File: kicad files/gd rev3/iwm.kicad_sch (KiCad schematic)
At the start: 24 parts, among them J2 DB19_4, J3 DB19_16, J4 EN, J5 DSUB19, J6 FDC Hdr, J7 EN, J8 EN, J9 Game Port, U11 IWM

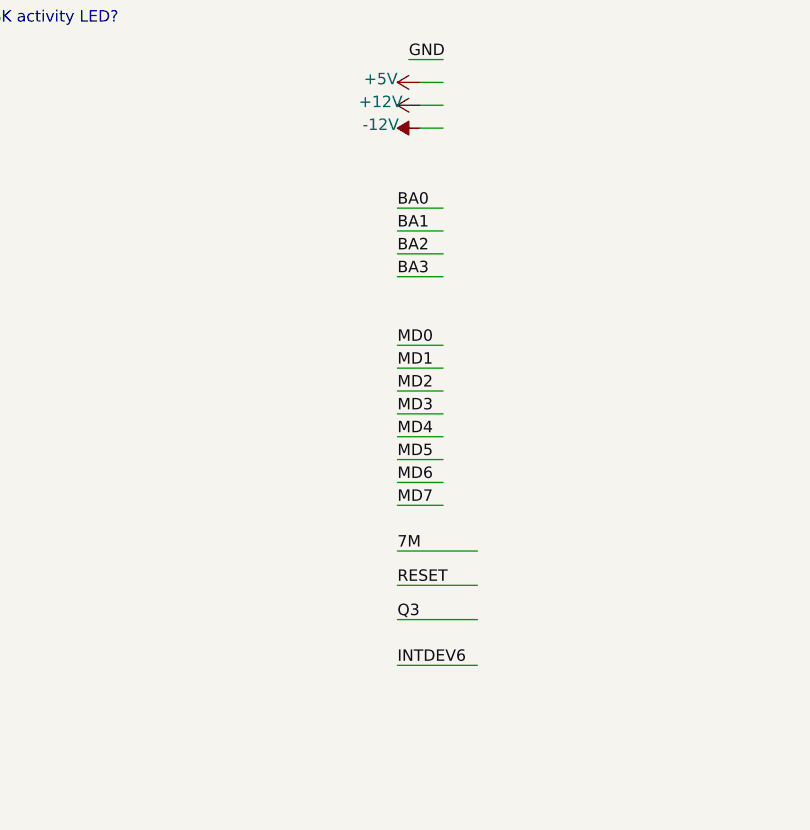
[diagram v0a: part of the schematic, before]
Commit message: ibom for audio and adding some hierarchical labels (wrong branch)
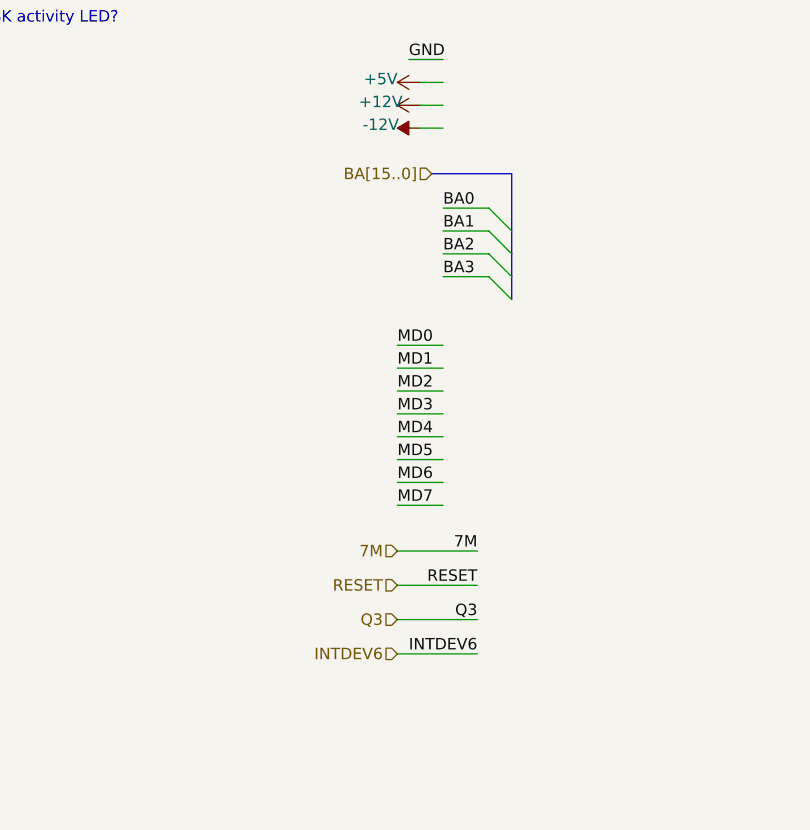
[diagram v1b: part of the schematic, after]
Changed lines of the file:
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@@
   )
   (no_connect (at 339.09 106.68))
+  (bus_entry (at 33.02 78.74) (size 2.54 2.54)
+    (stroke (width 0) (type default) (color 0 0 0 0))
+  )
+  (bus_entry (at 33.02 76.2) (size 2.54 2.54)
+    (stroke (width 0) (type default) (color 0 0 0 0))
+  )
+  (bus_entry (at 33.02 81.28) (size 2.54 2.54)
+    (stroke (width 0) (type default) (color 0 0 0 0))
+  )
+  (bus_entry (at 33.02 73.66) (size 2.54 2.54)
+    (stroke (width 0) (type default) (color 0 0 0 0))
+  )
   (wire (pts (xy 229.87 68.58) (xy 229.87 74.93))
     (stroke (width 0) (type default) (color 0 0 0 0))
@@
     (stroke (width 0) (type default) (color 0 0 0 0))
   )
-  (wire (pts (xy 22.86 76.2) (xy 27.94 76.2))
+  (wire (pts (xy 27.94 76.2) (xy 33.02 76.2))
     (stroke (width 0) (type default) (color 0 0 0 0))
   )
@@
     (stroke (width 0) (type default) (color 0 0 0 0))
   )
+  (bus (pts (xy 35.56 83.82) (xy 35.56 81.28))
+    (stroke (width 0) (type default) (color 0 0 0 0))
+  )
   (wire (pts (xy 201.93 110.49) (xy 212.09 110.49))
     (stroke (width 0) (type default) (color 0 0 0 0))
@@
     (stroke (width 0) (type default) (color 0 0 0 0))
   )
+  (bus (pts (xy 35.56 81.28) (xy 35.56 78.74))
+    (stroke (width 0) (type default) (color 0 0 0 0))
+  )
   (wire (pts (xy 209.55 102.87) (xy 209.55 105.41))
     (stroke (width 0) (type default) (color 0 0 0 0))
@@
     (stroke (width 0) (type default) (color 0 0 0 0))
   )
+  (bus (pts (xy 26.67 69.85) (xy 35.56 69.85))
+    (stroke (width 0) (type default) (color 0 0 0 0))
+  )
   (wire (pts (xy 227.33 53.34) (xy 227.33 60.96))
     (stroke (width 0) (type default) (color 0 0 0 0))
@@
     (stroke (width 0) (type default) (color 0 0 0 0))
   )
-  (wire (pts (xy 22.86 78.74) (xy 27.94 78.74))
+  (wire (pts (xy 27.94 78.74) (xy 33.02 78.74))
     (stroke (width 0) (type default) (color 0 0 0 0))
   )
@@
     (stroke (width 0) (type default) (color 0 0 0 0))
   )
+  (bus (pts (xy 35.56 76.2) (xy 35.56 69.85))
+    (stroke (width 0) (type default) (color 0 0 0 0))
+  )
   (wire (pts (xy 339.09 121.92) (xy 344.17 121.92))
     (stroke (width 0) (type default) (color 0 0 0 0))
@@
     (stroke (width 0) (type default) (color 0 0 0 0))
   )
-  (wire (pts (xy 22.86 81.28) (xy 27.94 81.28))
+  (wire (pts (xy 27.94 81.28) (xy 33.02 81.28))
     (stroke (width 0) (type default) (color 0 0 0 0))
   )
@@
     (stroke (width 0) (type default) (color 0 0 0 0))
   )
-  (wire (pts (xy 31.75 124.46) (xy 22.86 124.46))
+  (wire (pts (xy 31.75 123.19) (xy 22.86 123.19))
     (stroke (width 0) (type default) (color 0 0 0 0))
   )
@@
     (stroke (width 0) (type default) (color 0 0 0 0))
   )
+  (bus (pts (xy 35.56 78.74) (xy 35.56 76.2))
+    (stroke (width 0) (type default) (color 0 0 0 0))
+  )
   (wire (pts (xy 224.79 90.17) (xy 232.41 90.17))
     (stroke (width 0) (type default) (color 0 0 0 0))
@@
     (stroke (width 0) (type default) (color 0 0 0 0))
   )
-  (wire (pts (xy 22.86 73.66) (xy 27.94 73.66))
+  (wire (pts (xy 27.94 73.66) (xy 33.02 73.66))
     (stroke (width 0) (type default) (color 0 0 0 0))
   )
@@
     (effects (font (size 1.27 1.27)) (justify right bottom))
   )
-  (label "RESET" (at 22.86 115.57 0)
-    (effects (font (size 1.27 1.27)) (justify left bottom))
+  (label "RESET" (at 31.75 115.57 180)
+    (effects (font (size 1.27 1.27)) (justify right bottom))
   )
   (label "bWREQ" (at 229.87 60.96 90)
@@
     (effects (font (size 1.27 1.27)) (justify left bottom))
   )
-  (label "7M" (at 22.86 111.76 0)
-    (effects (font (size 1.27 1.27)) (justify left bottom))
+  (label "7M" (at 31.75 111.76 180)
+    (effects (font (size 1.27 1.27)) (justify right bottom))
   )
   (label "GND" (at 205.74 87.63 0)
@@
     (effects (font (size 1.27 1.27)) (justify right bottom))
   )
-  (label "BA1" (at 22.86 76.2 0)
+  (label "BA1" (at 27.94 76.2 0)
     (effects (font (size 1.27 1.27)) (justify left bottom))
   )
@@
     (effects (font (size 1.27 1.27)) (justify left bottom))
   )
-  (label "BA3" (at 22.86 81.28 0)
+  (label "BA3" (at 27.94 81.28 0)
     (effects (font (size 1.27 1.27)) (justify left bottom))
   )
@@
     (effects (font (size 1.27 1.27)) (justify right bottom))
   )
-  (label "BA0" (at 22.86 73.66 0)
+  (label "BA0" (at 27.94 73.66 0)
     (effects (font (size 1.27 1.27)) (justify left bottom))
   )
@@
     (effects (font (size 1.27 1.27)) (justify right bottom))
   )
-  (label "INTDEV6" (at 22.86 124.46 0)
-    (effects (font (size 1.27 1.27)) (justify left bottom))
+  (label "INTDEV6" (at 31.75 123.19 180)
+    (effects (font (size 1.27 1.27)) (justify right bottom))
   )
   (label "seek1" (at 143.51 101.6 180)
@@
     (effects (font (size 1.27 1.27)) (justify right bottom))
   )
-  (label "BA2" (at 22.86 78.74 0)
+  (label "BA2" (at 27.94 78.74 0)
     (effects (font (size 1.27 1.27)) (justify left bottom))
   )
@@
     (effects (font (size 1.27 1.27)) (justify right bottom))
   )
-  (label "Q3" (at 22.86 119.38 0)
-    (effects (font (size 1.27 1.27)) (justify left bottom))
+  (label "Q3" (at 31.75 119.38 180)
+    (effects (font (size 1.27 1.27)) (justify right bottom))
   )
   (label "PDL1" (at 344.17 121.92 180)
@@
     (effects (font (size 1.27 1.27)) (justify left bottom))
   )
+  (hierarchical_label "INTDEV6" (shape input) (at 22.86 123.19 180)
+    (effects (font (size 1.27 1.27)) (justify right))
+  )
+  (hierarchical_label "RESET" (shape input) (at 22.86 115.57 180)
+    (effects (font (size 1.27 1.27)) (justify right))
+  )
+  (hierarchical_label "Q3" (shape input) (at 22.86 119.38 180)
+    (effects (font (size 1.27 1.27)) (justify right))
+  )
+  (hierarchical_label "7M" (shape input) (at 22.86 111.76 180)
+    (effects (font (size 1.27 1.27)) (justify right))
+  )
+  (hierarchical_label "BA[15..0]" (shape input) (at 26.67 69.85 180)
+    (effects (font (size 1.27 1.27)) (justify right))
+  )
   (symbol (lib_id "power:+5V") (at 321.31 106.68 0) (unit 1)

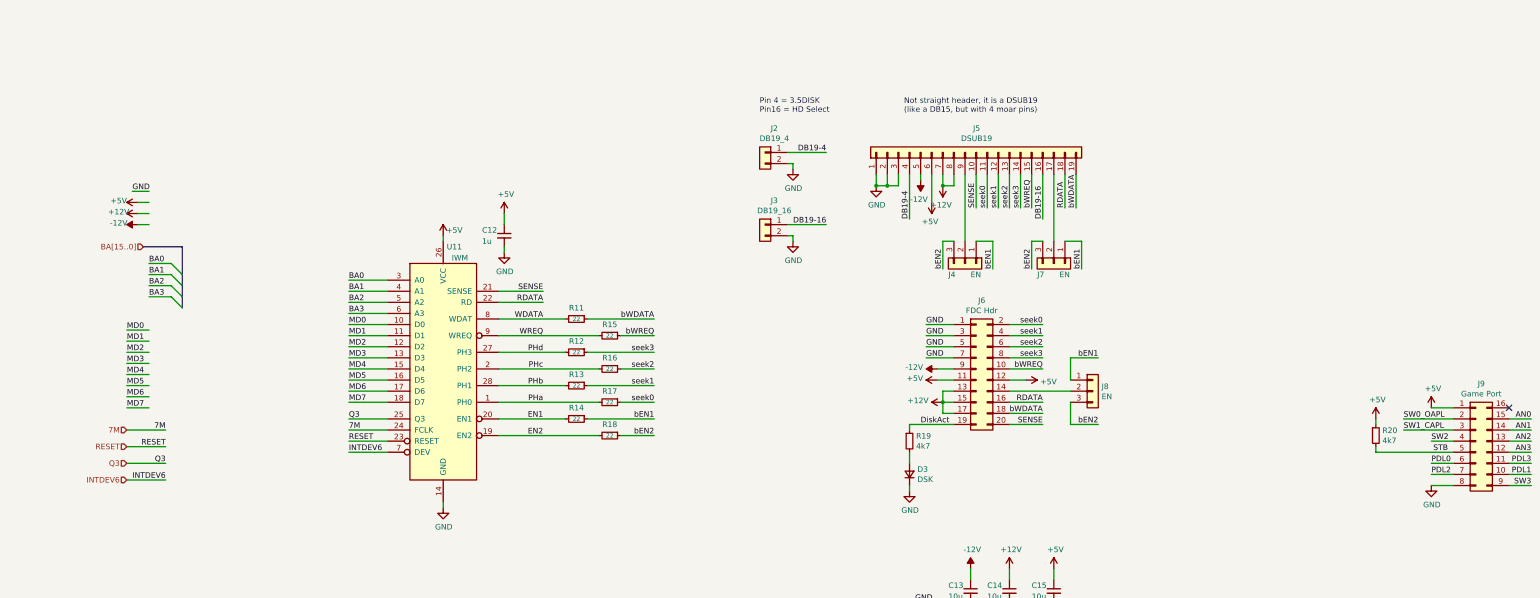
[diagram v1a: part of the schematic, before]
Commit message: initial slot/io breakout sheet labels
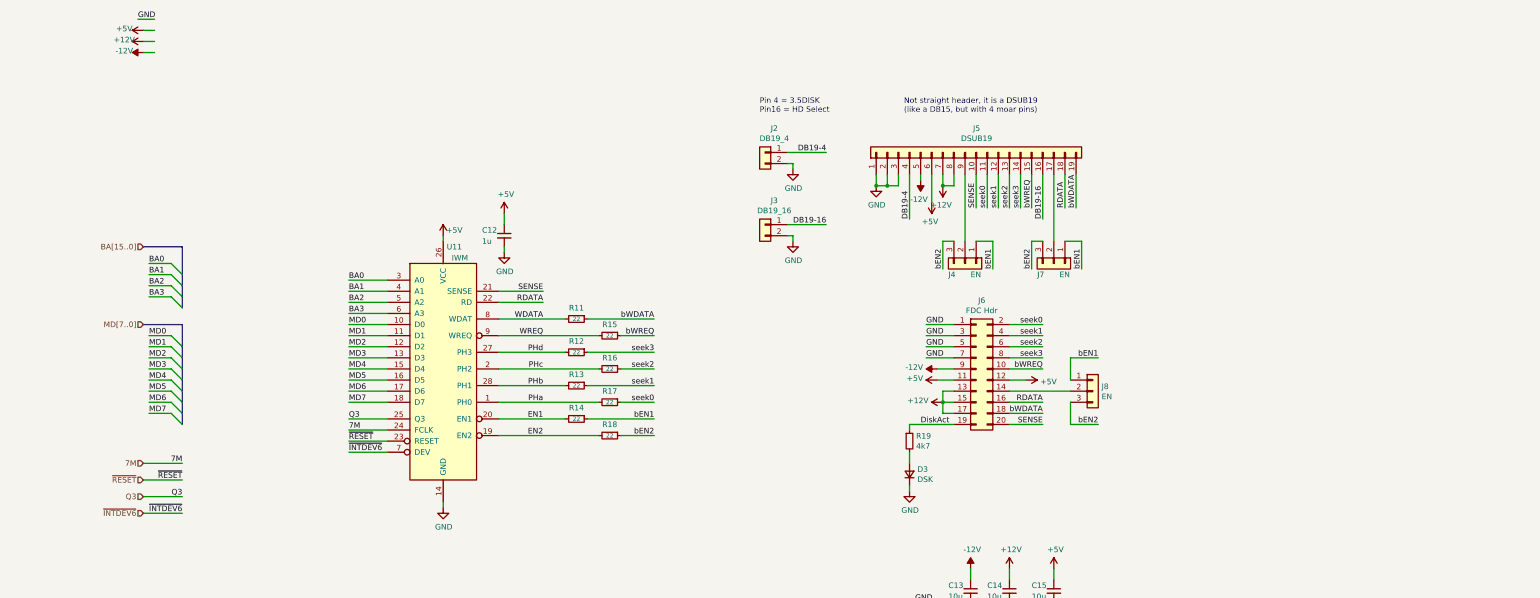
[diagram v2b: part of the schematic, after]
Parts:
- removed J9: Game Port, Package_DIP:DIP-16_W7.62mm_Socket, symbol Connector_Generic:Conn_02x08_Counter_Clockwise
- removed R20: 4k7, Resistor_SMD:R_0805_2012Metric, symbol My_Library:R_0805
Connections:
- net INTDEV6 renamed ~{INTDEV6}
- net RESET renamed ~{RESET}
- no-connect marks 1 -> 0

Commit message: after crash commit. arranging high-level sheet signals (and added audio circuit)
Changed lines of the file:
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@@
-    (stroke (width 0) (type default) (color 0 0 0 0))
-  )
-  (wire (pts (xy 25.4 17.78) (xy 29.21 17.78))
     (stroke (width 0) (type default) (color 0 0 0 0))
   )
@@
     (stroke (width 0) (type default) (color 0 0 0 0))
   )
-  (wire (pts (xy 29.21 25.4) (xy 26.67 25.4))
-    (stroke (width 0) (type default) (color 0 0 0 0))
-  )
   (wire (pts (xy 201.93 110.49) (xy 201.93 111.76))
     (stroke (width 0) (type default) (color 0 0 0 0))
@@
     (stroke (width 0) (type default) (color 0 0 0 0))
   )
-  (wire (pts (xy 26.67 22.86) (xy 29.21 22.86))
-    (stroke (width 0) (type default) (color 0 0 0 0))
-  )
   (wire (pts (xy 209.55 68.58) (xy 209.55 74.93))
     (stroke (width 0) (type default) (color 0 0 0 0))
@@
   )
   (wire (pts (xy 229.87 53.34) (xy 229.87 60.96))
-    (stroke (width 0) (type default) (color 0 0 0 0))
-  )
-  (wire (pts (xy 29.21 20.32) (xy 26.67 20.32))
     (stroke (width 0) (type default) (color 0 0 0 0))
   )
@@
   )
   (label "~{RESET}" (at 73.66 114.3 0)
-    (effects (font (size 1.27 1.27)) (justify left bottom))
-  )
-  (label "GND" (at 25.4 17.78 0)
     (effects (font (size 1.27 1.27)) (justify left bottom))
   )
@@
     )
     (property "Datasheet" "" (id 3) (at 109.22 62.23 0)
-      (effects (font (size 1.27 1.27)) hide)
-    )
-    (pin "1")
-  )
-  (symbol (lib_id "power:-12V") (at 26.67 25.4 90) (unit 1)
-    (in_bom yes) (on_board yes)
-    (property "Reference" "#PWR0181" (id 0) (at 24.13 25.4 0)
-      (effects (font (size 1.27 1.27)) hide)
-    )
-    (property "Value" "-12V" (id 1) (at 22.2758 25.019 90))
-    (property "Footprint" "" (id 2) (at 26.67 25.4 0)
-      (effects (font (size 1.27 1.27)) hide)
-    )
-    (property "Datasheet" "" (id 3) (at 26.67 25.4 0)
-      (effects (font (size 1.27 1.27)) hide)
-    )
-    (pin "1")
-  )
-  (symbol (lib_id "power:+12V") (at 26.67 22.86 90) (unit 1)
-    (in_bom yes) (on_board yes)
-    (property "Reference" "#PWR0180" (id 0) (at 30.48 22.86 0)
-      (effects (font (size 1.27 1.27)) hide)
-    )
-    (property "Value" "+12V" (id 1) (at 22.2758 22.479 90))
-    (property "Footprint" "" (id 2) (at 26.67 22.86 0)
-      (effects (font (size 1.27 1.27)) hide)
-    )
-    (property "Datasheet" "" (id 3) (at 26.67 22.86 0)
       (effects (font (size 1.27 1.27)) hide)
     )
@@
     (pin "9")
   )
-  (symbol (lib_id "power:+5V") (at 26.67 20.32 90) (unit 1)
-    (in_bom yes) (on_board yes)
-    (property "Reference" "#PWR0179" (id 0) (at 30.48 20.32 0)
-      (effects (font (size 1.27 1.27)) hide)
-    )
-    (property "Value" "+5V" (id 1) (at 22.2758 19.939 90))
-    (property "Footprint" "" (id 2) (at 26.67 20.32 0)
-      (effects (font (size 1.27 1.27)) hide)
-    )
-    (property "Datasheet" "" (id 3) (at 26.67 20.32 0)
-      (effects (font (size 1.27 1.27)) hide)
-    )
-    (pin "1")
-  )
   (symbol (lib_id "power:GND") (at 194.31 55.88 0) (unit 1)

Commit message: added missing Flash to 2040 circuits and sync'd title blocks
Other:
- company: (none) -> twitch.tv/baldengineer
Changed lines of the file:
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@@
 (kicad_sch (version 20211123) (generator eeschema)
   (paper "A4")
+  (title_block
+    (rev "3a")
+    (company "twitch.tv/baldengineer")
+  )
   (junction (at 209.55 105.41) (diameter 0) (color 0 0 0 0)
   )

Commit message: ERC clean-up
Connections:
- net GND: now also J5.0

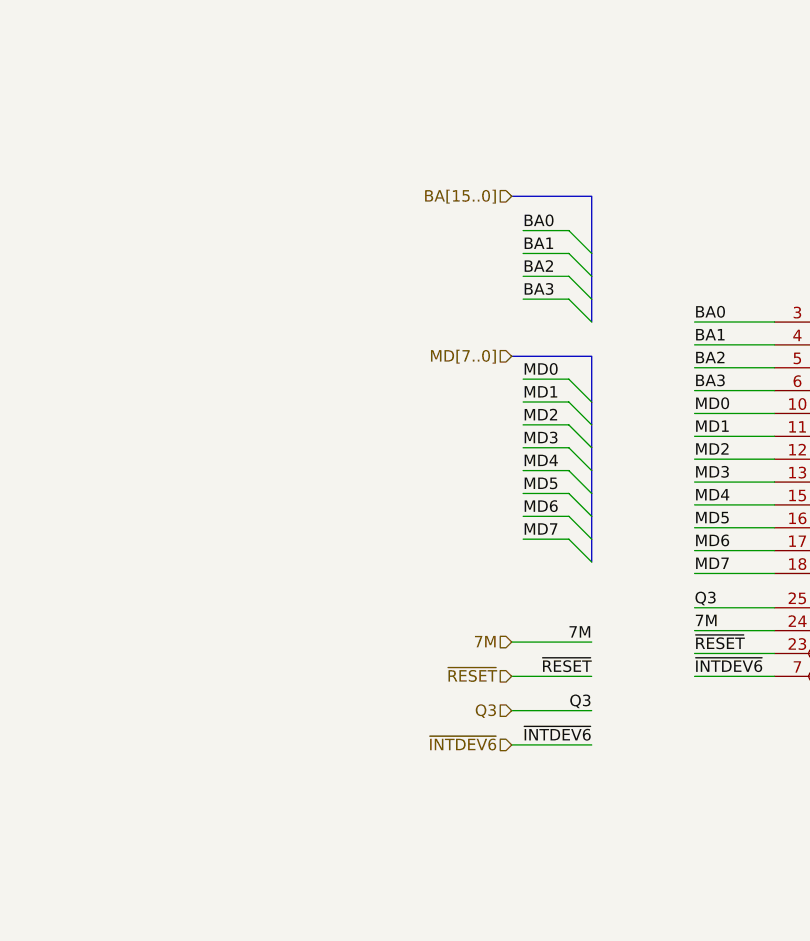
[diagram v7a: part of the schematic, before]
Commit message: colorized multi-sheet, other minor changes
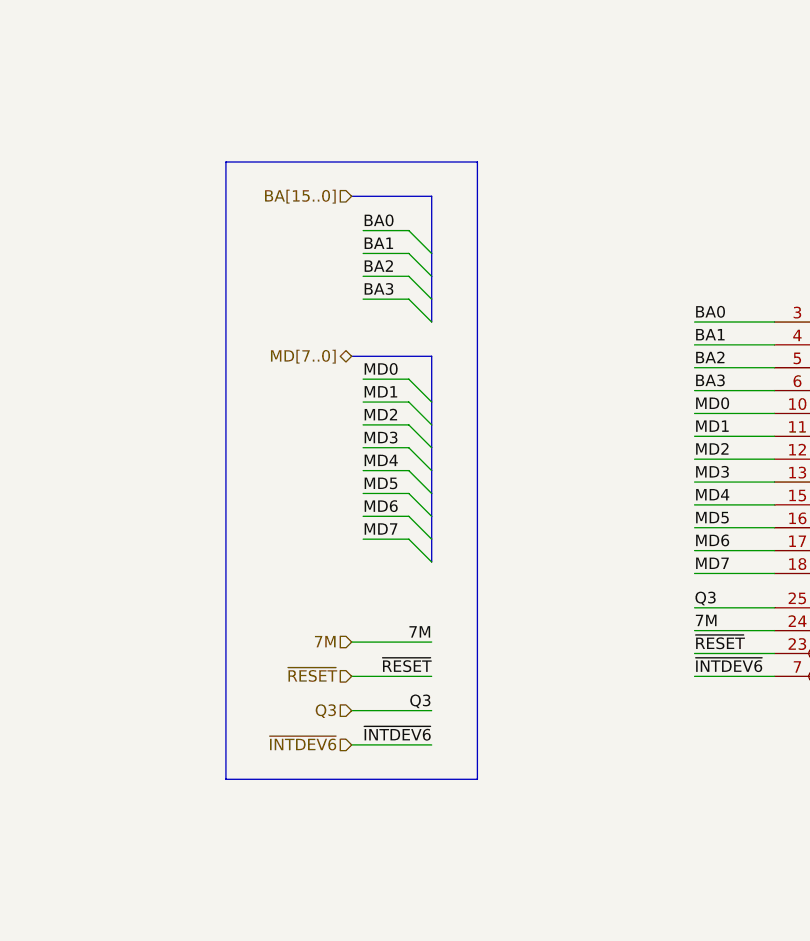
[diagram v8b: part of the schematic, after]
